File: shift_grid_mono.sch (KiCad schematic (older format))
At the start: 23 parts, among them J1 Conn_01x08, U1 74HC595, U2 74HC595

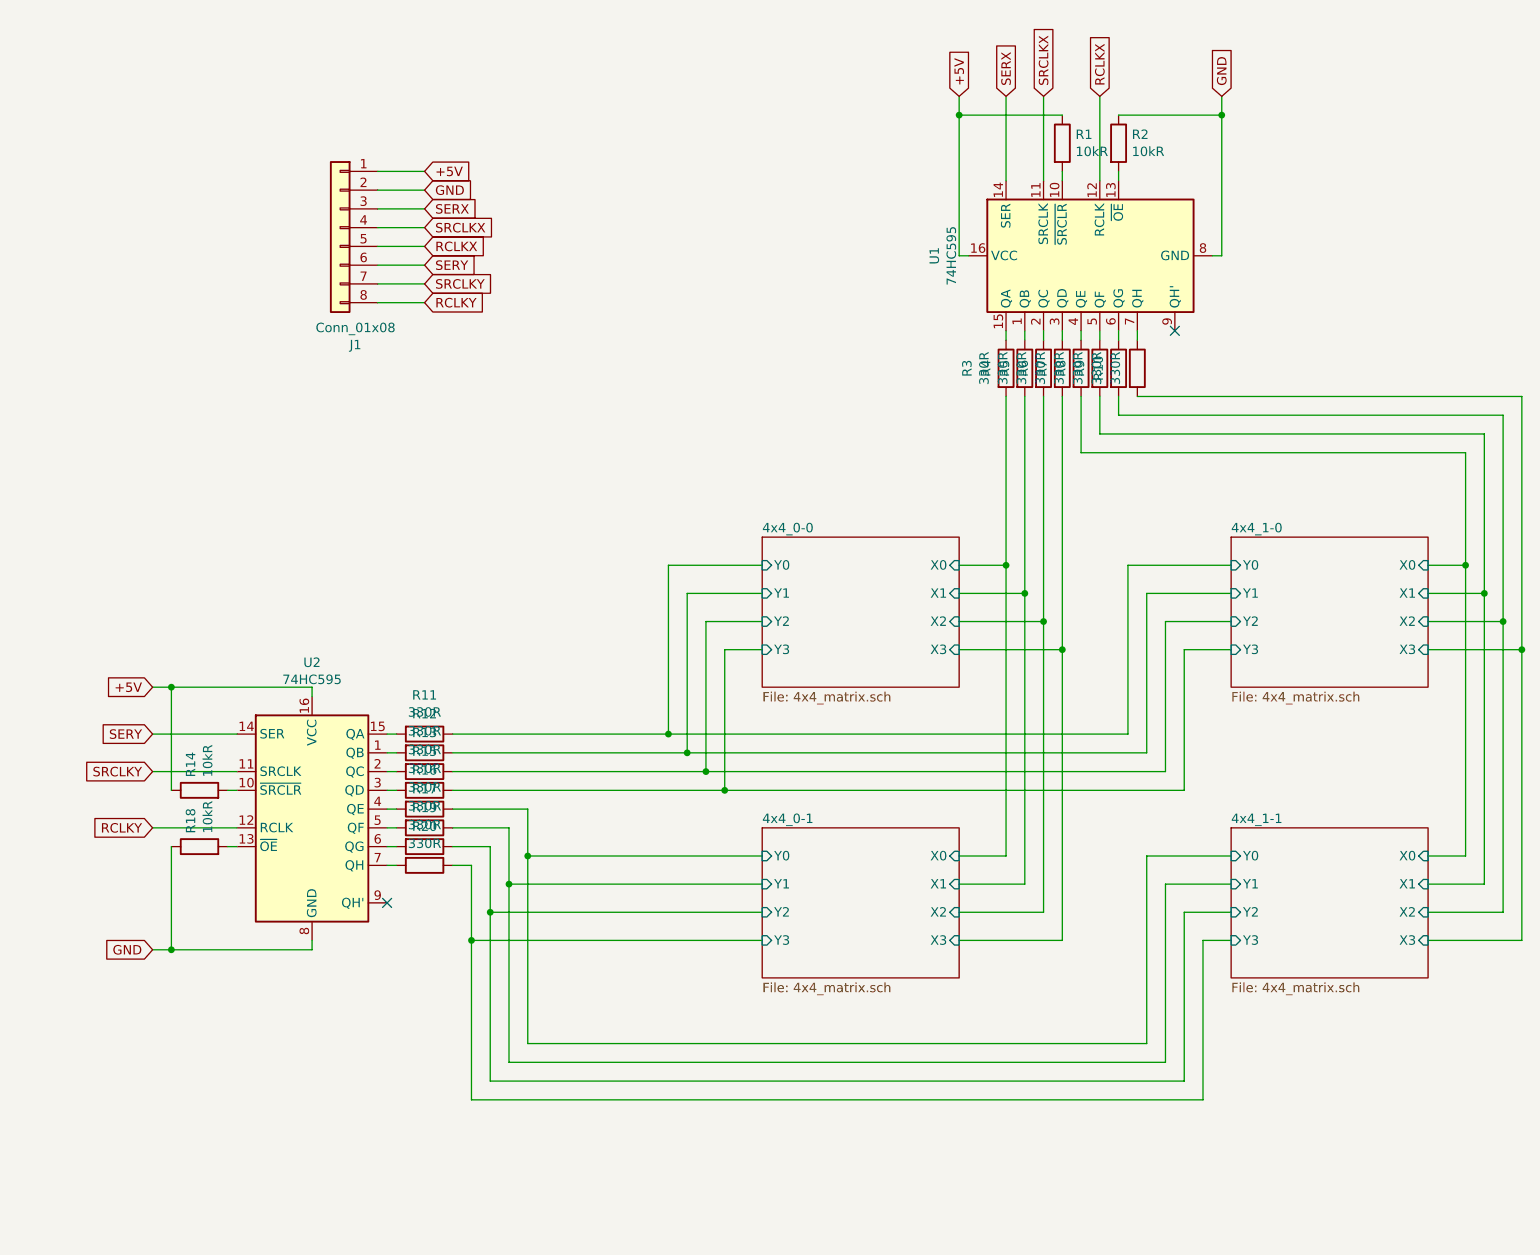
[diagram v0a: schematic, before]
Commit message: Reduce LEDs by half
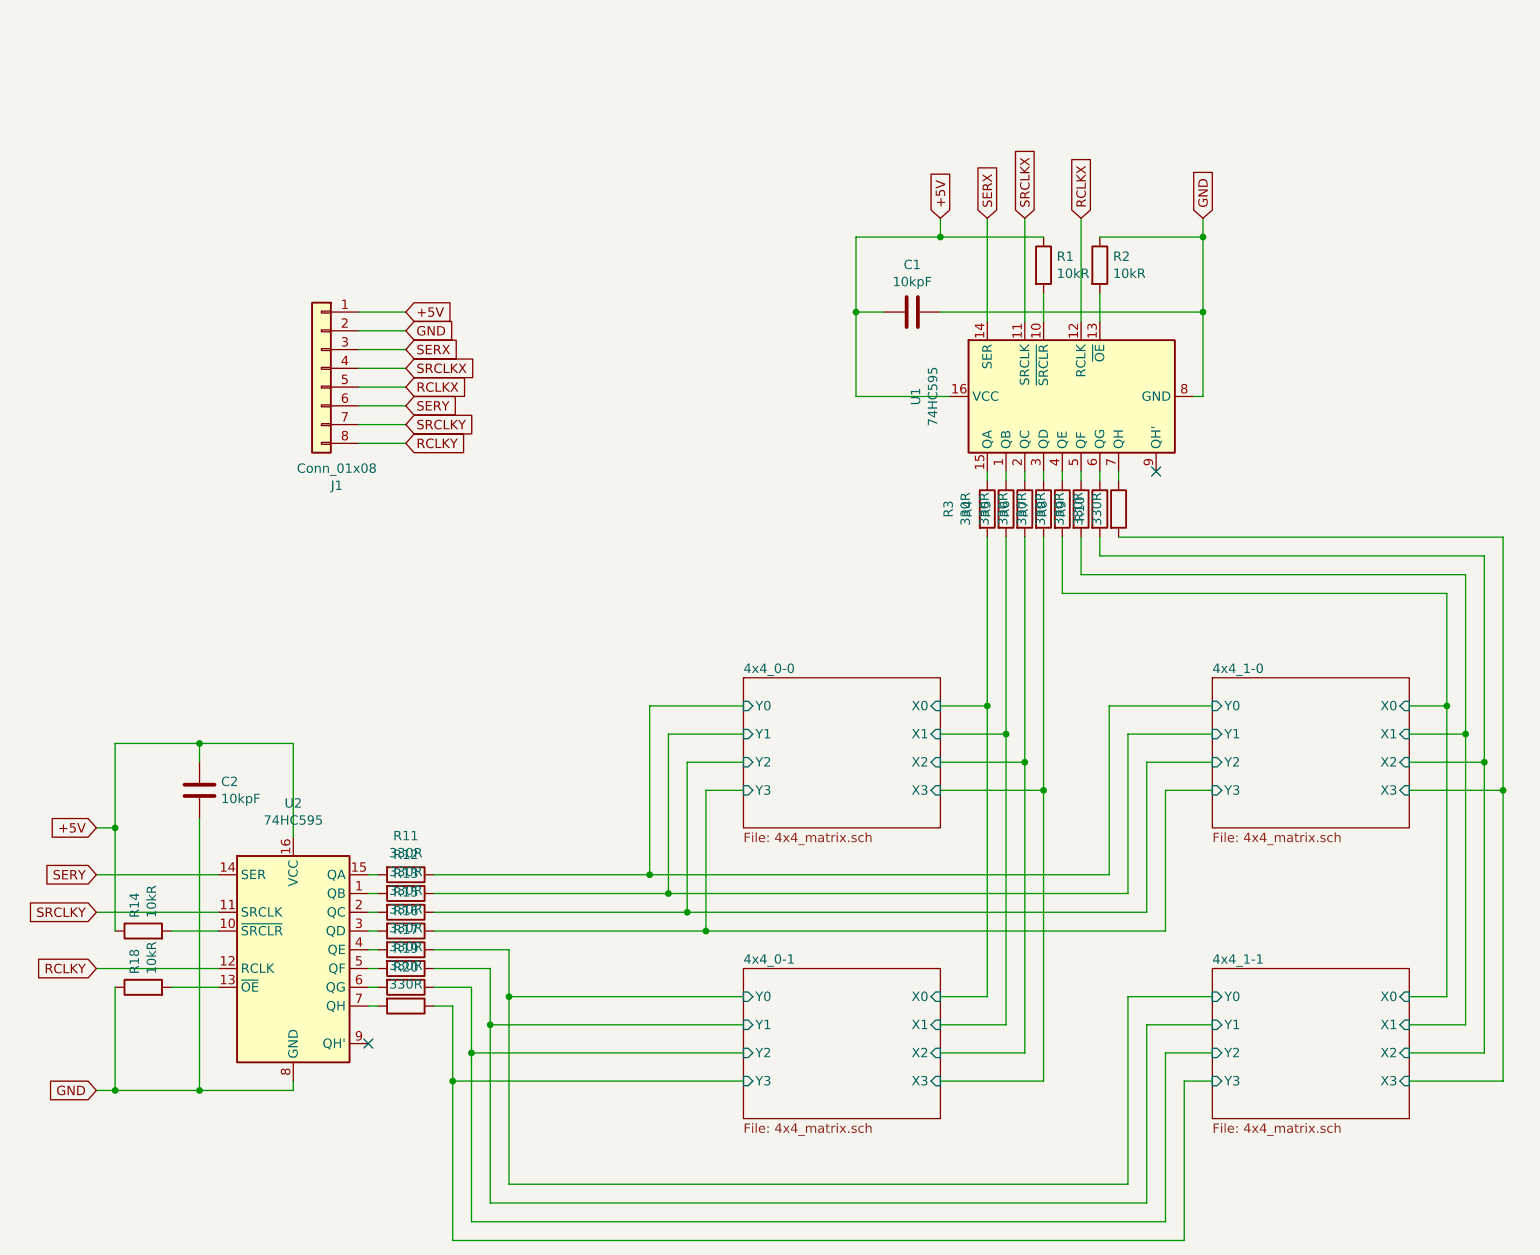
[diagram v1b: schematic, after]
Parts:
- added C1, C2: 10kpF, Capacitor_SMD:C_0805_2012Metric, symbol Device:C
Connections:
- net +5V: now also C1.2, C2.1
- net GND: now also C1.1, C2.2
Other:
- moved on the sheet: J1, R1, R10, R11, R12, R13, R14, R15, R16, R17, R18, R19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
